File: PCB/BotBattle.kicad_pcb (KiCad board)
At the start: 2 copper layers, 7 parts, among them J1 Screw_Terminal_01x04, J2 Screw_Terminal_01x04, J3 Conn_02x20_Odd_Even, J4 Screw_Terminal_01x03, J5 Screw_Terminal_01x02

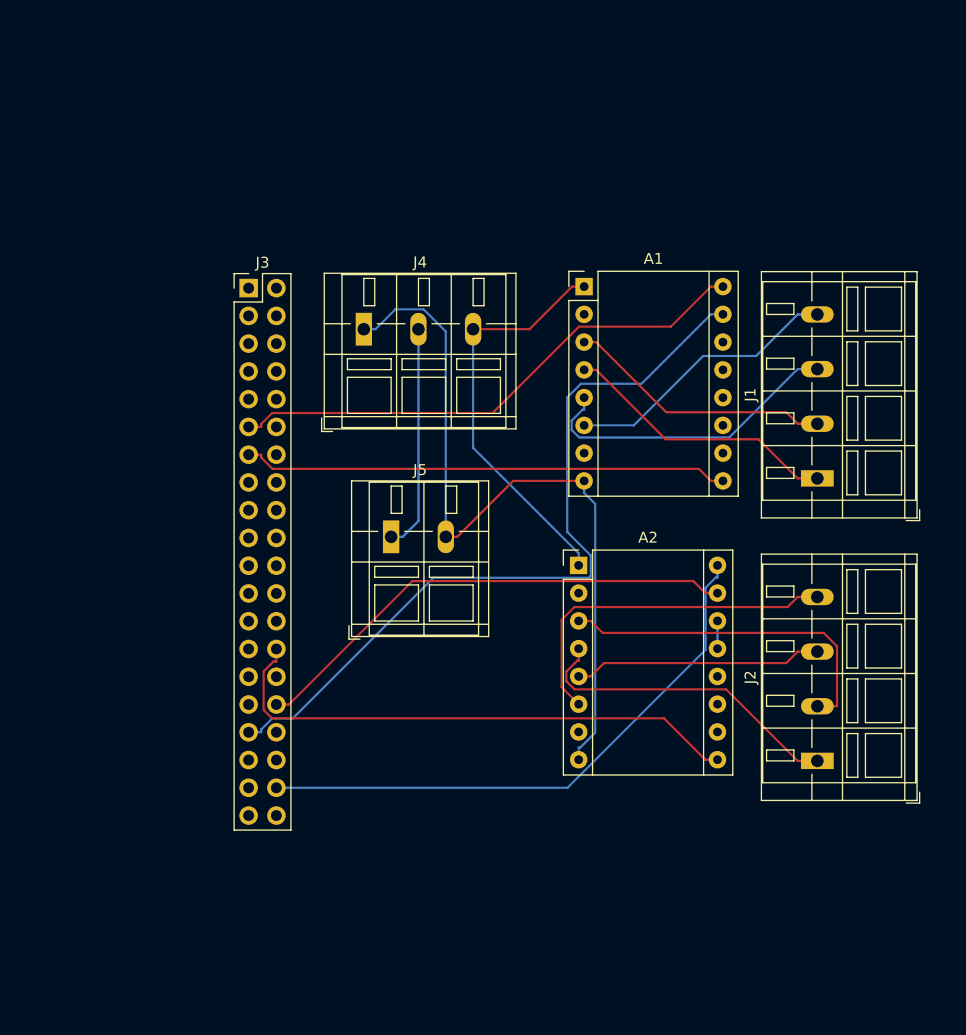
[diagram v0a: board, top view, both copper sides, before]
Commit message: Commit Type: Enhacement
- Added volt masurment system

Signed-off-by: ButrosGroot <butrosgroot@gmail.com>
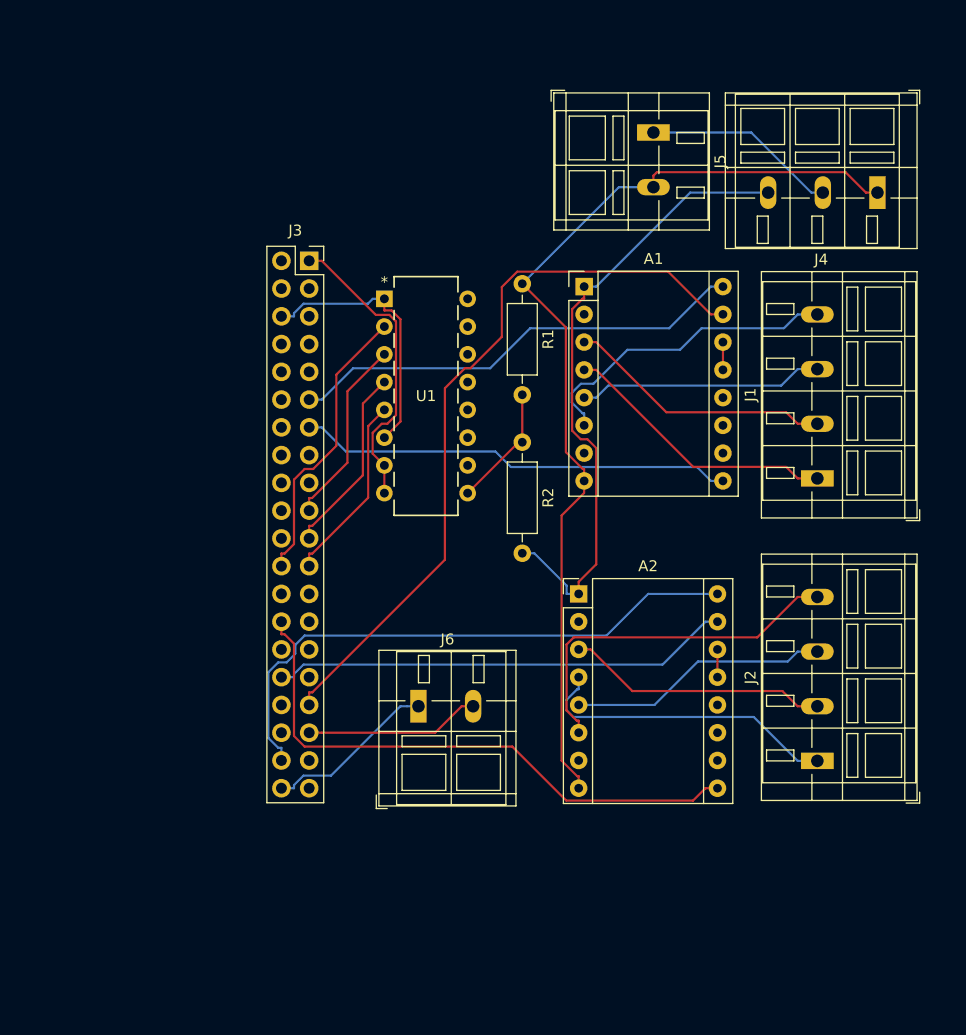
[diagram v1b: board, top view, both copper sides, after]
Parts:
- added J6: Screw_Terminal_01x02, TerminalBlock_WAGO:TerminalBlock_WAGO_236-102_1x02_P5.00mm_45Degree, F.Cu at (164.0, 110.5)
- added R1: 17,5K, Resistor_THT:R_Axial_DIN0207_L6.3mm_D2.5mm_P10.16mm_Horizontal, F.Cu at (173.5, 71.8)
- added R2: 4,7k, Resistor_THT:R_Axial_DIN0207_L6.3mm_D2.5mm_P10.16mm_Horizontal, F.Cu at (173.5, 86.3)
- added U1: MCP3008-I/P, Ultra Librarian:PDIP16_300MC_MCH, F.Cu at (160.9, 73.2)
- J3: footprint Connector_PinHeader_2.54mm:PinHeader_2x20_P2.54mm_Vertical -> Connector_PinSocket_2.54mm:PinSocket_2x20_P2.54mm_Vertical
- moved J4 48.6 mm to (206.0, 63.5), turned to 180 degrees
- moved J5 44.1 mm to (185.5, 58.0), turned to -90 degrees
- moved J3 6.08 mm to (154.0, 69.7)
- moved A2 2.61 mm to (178.7, 100.2)
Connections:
- A1 pad 13: unconnected-(A1-~{RST}-Pad13) -> Net-(A1-~{RST})
- A1 pad 14: unconnected-(A1-~{SLP}-Pad14) -> Net-(A1-~{RST})
- J3 pad 1: unconnected-(J3-3v3_power-Pad1) -> Net-(J3-3v3_power)
- J3 pad 19: unconnected-(J3-Pin_19-Pad19) -> Net-(J3-Pin_19)
- J3 pad 21: unconnected-(J3-Pin_21-Pad21) -> Net-(J3-Pin_21)
- J3 pad 23: unconnected-(J3-Pin_23-Pad23) -> Net-(J3-Pin_23)
- J3 pad 24: unconnected-(J3-Pin_24-Pad24) -> Net-(J3-Pin_24)
- J3 pad 35: unconnected-(J3-Pin_35-Pad35) -> Net-(J3-Pin_35)
- J3 pad 40: unconnected-(J3-Pin_40-Pad40) -> Net-(J3-Pin_40)
- J3 pad 6: unconnected-(J3-Pin_6-Pad6) -> Net-(J3-Pin_6)
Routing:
- net Net-(J3-3v3_power): track 0.00 -> 27.6 mm
- net Net-(J3-Pin_24): track 0.00 -> 26.5 mm
- net Net-(J3-Pin_6): track 0.00 -> 24.6 mm
- net Net-(J4-Pin_3): track 37.4 -> 58.2 mm
- net Net-(A1-VMOT): track 69.3 -> 88.3 mm
- net Net-(J3-Pin_23): track 0.00 -> 17.3 mm
- net Net-(J3-Pin_21): track 0.00 -> 17.3 mm
- net Net-(J3-Pin_19): track 0.00 -> 17.3 mm
- net Net-(J3-Pin_35): track 0.00 -> 16.0 mm
- net Net-(J3-Pin_40): track 0.00 -> 15.8 mm
- net Net-(R1-Pad2): track 0.00 -> 11.3 mm
- net Net-(A2-A2): track 31.9 -> 24.0 mm
- net Net-(A1-DIR): track 48.9 -> 42.1 mm
- net Net-(A1-B1): track 28.9 -> 22.4 mm
- net Net-(A1-~{EN}): track 44.6 -> 39.9 mm
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
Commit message: Commit Type: Enhancement
- Changed trace width to handel A over the line

Signed-off-by: ButrosGroot <butrosgroot@gmail.com>
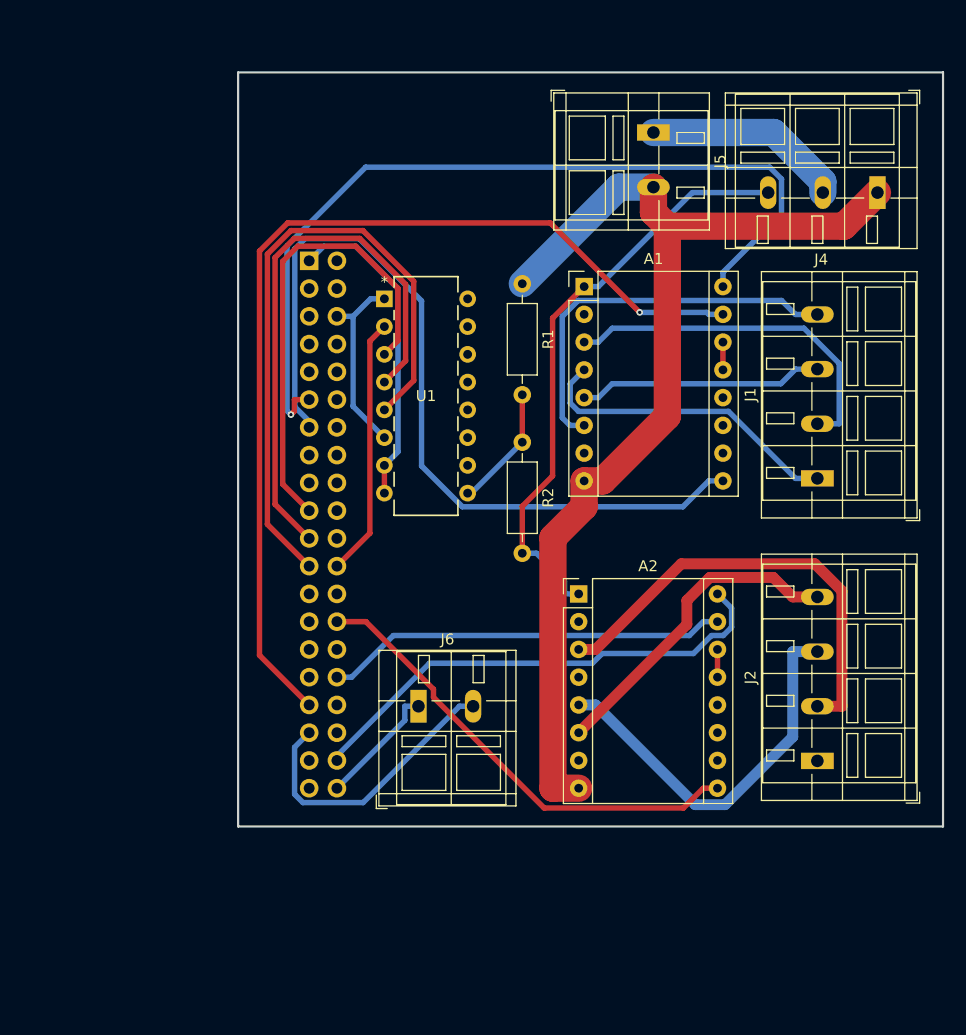
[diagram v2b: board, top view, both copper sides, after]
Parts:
- J3: moved to B.Cu
- turned J3 to 180 degrees
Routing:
- net Net-(J3-Pin_23): track 17.3 -> 59.2 mm
- net Net-(A1-DIR): track 42.1 -> 79.2 mm, vias 0 -> 1
- net Net-(A1-~{EN}): track 39.9 -> 76.4 mm
- net Net-(J3-Pin_21): track 17.3 -> 51.1 mm
- net Net-(A2-A1): track 28.4 -> 0.00 mm
- net Net-(J3-Pin_19): track 17.3 -> 43.1 mm
- net Net-(A1-STEP): track 68.4 -> 90.4 mm, vias 0 -> 1
- net Net-(A2-A2): track 24.0 -> 41.2 mm
- net Net-(A2-B1): track 23.9 -> 36.0 mm
- net Net-(A1-VMOT): track 88.3 -> 99.4 mm
- net Net-(J3-Pin_35): track 16.0 -> 26.5 mm
- net Net-(A2-~{EN}): track 52.8 -> 43.1 mm
- net Net-(A1-A2): track 24.4 -> 32.7 mm
- net Net-(A2-DIR): track 53.3 -> 45.0 mm
- net Net-(J3-Pin_6): track 24.6 -> 17.3 mm
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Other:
- board outline added: 64.5 x 69 mm

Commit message: Commit Type: Enhacment
- Added naming to screw terminals
- changed the position of the dvr

Signed-off-by: ButrosGroot <ButrosGroot@gmail.com>
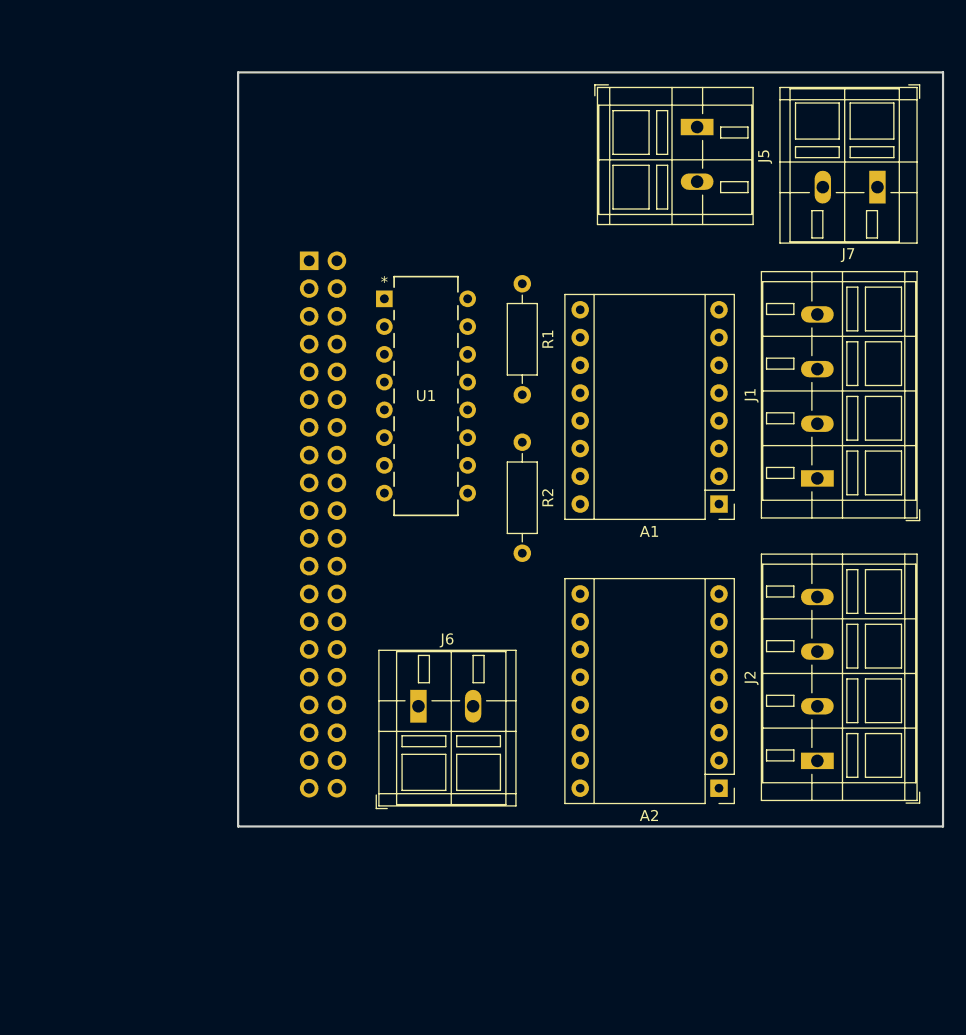
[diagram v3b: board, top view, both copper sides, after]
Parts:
- removed J4: Screw_Terminal_01x03, TerminalBlock_WAGO:TerminalBlock_WAGO_236-103_1x03_P5.00mm_45Degree
- added J7: ingang_lipo, TerminalBlock_WAGO:TerminalBlock_WAGO_236-102_1x02_P5.00mm_45Degree, F.Cu at (206.0, 63.0)
- J1, J2: value Screw_Terminal_01x04 -> uit_Nema_17
- J5: value Screw_Terminal_01x02 -> uit_buck_converter_raspberry_pi
- U1: footprint Ultra Librarian:PDIP16_300MC_MCH -> MCP3008-I-P:PDIP16_300MC_MCH
- moved A1 23.4 mm to (191.5, 92.0), turned to 180 degrees
- moved A2 21.9 mm to (191.5, 118.0), turned to 180 degrees
- moved J5 4.03 mm to (189.5, 57.5)
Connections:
- A1 pad 1: Net-(J4-Pin_3) -> GND
- A2 pad 1: Net-(J4-Pin_3) -> GND
- J5 pad 1: Net-(J4-Pin_2) -> GND
- R2 pad 2: Net-(J4-Pin_3) -> GND
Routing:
- net Net-(A1-VMOT): track 99.4 -> 0.00 mm
- net Net-(A1-STEP): track 90.4 -> 0.00 mm, vias 1 -> 0
- net Net-(A1-DIR): track 79.2 -> 0.00 mm, vias 1 -> 0
- net Net-(A1-~{EN}): track 76.4 -> 0.00 mm
- net Net-(J3-Pin_23): track 59.2 -> 0.00 mm
- net Net-(J4-Pin_3): track 54.5 -> 0.00 mm
- net Net-(J3-Pin_21): track 51.1 -> 0.00 mm
- net Net-(A2-DIR): track 45.0 -> 0.00 mm
- net Net-(J3-Pin_19): track 43.1 -> 0.00 mm
- net Net-(A2-~{EN}): track 43.1 -> 0.00 mm
- net Net-(A2-A2): track 41.2 -> 0.00 mm
- net Net-(A2-STEP): track 36.9 -> 0.00 mm
- net Net-(A1-B2): track 36.0 -> 0.00 mm
- net Net-(A2-B1): track 36.0 -> 0.00 mm
- net Net-(A1-A2): track 32.7 -> 0.00 mm
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
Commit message: Commit Type: Enhacement
- PCB layout changes
- mounting holes added

Signed-off-by: ButrosGroot <ButrosGroot@gmail.com>
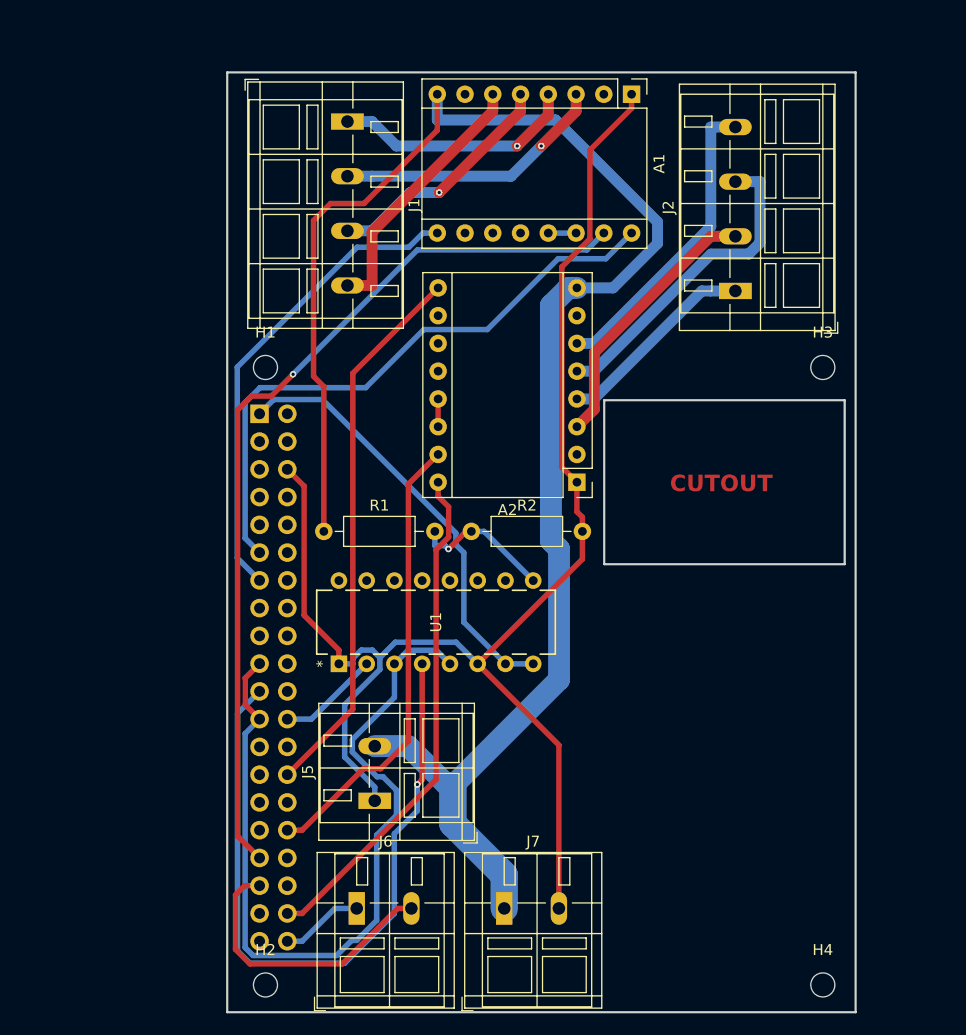
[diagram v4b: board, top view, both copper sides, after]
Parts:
- added H1: MountingHole, MountingHole:MountingHole_2.2mm_M2, F.Cu at (150.0, 79.5)
- added H2: MountingHole, MountingHole:MountingHole_2.2mm_M2, F.Cu at (150.0, 136.0)
- added H3: MountingHole, MountingHole:MountingHole_2.2mm_M2, F.Cu at (201.0, 79.5)
- added H4: MountingHole, MountingHole:MountingHole_2.2mm_M2, F.Cu at (201.0, 136.0)
- moved J7 74.3 mm to (171.8, 129.0), turned to 0 degrees
- moved J5 68.3 mm to (160.0, 119.2), turned to 90 degrees
- moved J1 54.0 mm to (157.5, 57.0), turned to -90 degrees
- moved J2 43.6 mm to (193.0, 72.5)
- moved A1 38.3 mm to (183.5, 54.5), turned to -90 degrees
- moved U1 33.7 mm to (156.7, 106.6), turned to 90 degrees
- moved A2 30.9 mm to (178.5, 90.0)
- moved R1 29.0 mm to (155.3, 94.5), turned to 0 degrees
- moved J6 19.3 mm to (158.3, 129.0)
- moved J3 14.7 mm to (149.5, 83.7)
- moved R2 9.40 mm to (168.8, 94.5), turned to 0 degrees
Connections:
- J3 pad 23: Net-(J3-Pin_23) -> Net-(J3-Pin_19)
- J3 pad 6: Net-(J3-Pin_6) -> GND
- U1 pad 1: Net-(J3-Pin_6) -> GND
- U1 pad 5: Net-(J3-Pin_23) -> Net-(J3-Pin_19)
- U1 pad 6: Net-(J3-Pin_6) -> GND
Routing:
- net Net-(A1-VMOT): track 0.00 -> 157.7 mm
- net GND: track 0.00 -> 135.5 mm
- net Net-(A1-STEP): track 0.00 -> 82.0 mm, vias 0 -> 1
- net Net-(J3-Pin_19): track 0.00 -> 75.2 mm
- net Net-(J3-Pin_21): track 0.00 -> 65.2 mm, vias 0 -> 1
- net Net-(A1-DIR): track 0.00 -> 56.1 mm
- net Net-(A2-~{EN}): track 0.00 -> 50.3 mm
- net Net-(A2-DIR): track 0.00 -> 46.8 mm
- net Net-(A1-~{EN}): track 0.00 -> 43.7 mm
- net Net-(A2-STEP): track 0.00 -> 41.8 mm
- net Net-(J3-3v3_power): track 0.00 -> 39.9 mm
- net Net-(A2-B1): track 0.00 -> 29.5 mm
- net Net-(A2-B2): track 0.00 -> 28.0 mm
- net Net-(J3-Pin_35): track 0.00 -> 26.3 mm
- net Net-(A1-A2): track 0.00 -> 24.9 mm, vias 0 -> 1
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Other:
- board size 64.5 x 69 mm -> 57.5 x 86 mm
- board text added: "CUTOUT"

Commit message: Commit Type: Enhacment
- Commited the final version of the pcb design

Signed-off-by: ButrosGroot <butrosgroot@gmail.com>
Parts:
- U1: footprint MCP3008-I-P:PDIP16_300MC_MCH -> Ultra Librarian:PDIP16_300MC_MCH
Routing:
- net GND: track 135.5 -> 0.00 mm
- net Net-(A2-A2): track 24.7 -> 33.3 mm
- net Net-(R1-Pad2): track 13.0 -> 13.9 mm
- net Net-(J3-Pin_21): track 65.2 -> 65.8 mm
- net Net-(J3-Pin_19): track 75.2 -> 75.3 mm, vias 0 -> 1
- net Net-(A1-VMOT): vias 0 -> 2
- added copper zone on B.Cu, net GND
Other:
- board size 57.5 x 86 mm -> 60.5 x 86 mm
